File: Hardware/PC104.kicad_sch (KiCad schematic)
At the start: 13 parts, among them J2 ESQ-126-14-G-D, J3 ESQ-126-14-G-D

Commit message: STM32 RTC
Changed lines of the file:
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@@
 	)
 	(junction
-		(at 248.92 88.9)
+		(at 251.46 88.9)
 		(diameter 0)
 		(color 0 0 0 0)
@@
 	)
 	(junction
-		(at 207.01 160.02)
+		(at 251.46 96.52)
 		(diameter 0)
 		(color 0 0 0 0)
 	)
 	(junction
-		(at 125.73 83.82)
+		(at 207.01 160.02)
 		(diameter 0)
 		(color 0 0 0 0)
 	)
 	(junction
-		(at 248.92 81.28)
+		(at 125.73 83.82)
 		(diameter 0)
 		(color 0 0 0 0)
 	)
 	(junction
-		(at 248.92 96.52)
+		(at 251.46 81.28)
 		(diameter 0)
 		(color 0 0 0 0)
@@
 	(wire
 		(pts
-			(xy 248.92 81.28) (xy 260.35 81.28)
+			(xy 251.46 81.28) (xy 260.35 81.28)
 		)
 		(stroke
@@
 	(wire
 		(pts
-			(xy 246.38 96.52) (xy 248.92 96.52)
+			(xy 246.38 96.52) (xy 251.46 96.52)
 		)
 		(stroke
@@
 	(wire
 		(pts
-			(xy 246.38 81.28) (xy 248.92 81.28)
+			(xy 246.38 81.28) (xy 251.46 81.28)
 		)
 		(stroke
@@
 	(wire
 		(pts
-			(xy 248.92 96.52) (xy 260.35 96.52)
-		)
-		(stroke
-			(width 0)
-			(type default)
-		)
-	)
-	(wire
-		(pts
 			(xy 198.12 177.8) (xy 198.12 180.34)
 		)
@@
 	(wire
 		(pts
-			(xy 246.38 88.9) (xy 248.92 88.9)
+			(xy 246.38 88.9) (xy 251.46 88.9)
 		)
 		(stroke
@@
 	(wire
 		(pts
+			(xy 251.46 96.52) (xy 260.35 96.52)
+		)
+		(stroke
+			(width 0)
+			(type default)
+		)
+	)
+	(wire
+		(pts
 			(xy 288.29 88.9) (xy 288.29 96.52)
 		)
@@
 	(wire
 		(pts
-			(xy 248.92 88.9) (xy 260.35 88.9)
+			(xy 251.46 88.9) (xy 260.35 88.9)
 		)
 		(stroke
@@
 	(wire
 		(pts
-			(xy 240.03 116.84) (xy 240.03 123.19)
+			(xy 240.03 116.84) (xy 240.03 121.92)
 		)
 		(stroke
@@
 	(hierarchical_label "VBAT_MONITOR"
 		(shape input)
-		(at 240.03 123.19 180)
+		(at 240.03 121.92 180)
 		(effects
 			(font
@@
 	(symbol
 		(lib_id "power:PWR_FLAG")
-		(at 248.92 96.52 0)
+		(at 251.46 96.52 0)
 		(unit 1)
 		(exclude_from_sim no)
@@
 		(fields_autoplaced yes)
 		(property "Reference" "#FLG04"
-			(at 248.92 94.615 0)
+			(at 251.46 94.615 0)
 			(effects
 				(font
@@
 		)
 		(property "Value" "PWR_FLAG"
-			(at 248.92 91.44 0)
+			(at 251.46 91.44 0)
 			(effects
 				(font
@@
 		)
 		(property "Footprint" ""
-			(at 248.92 96.52 0)
+			(at 251.46 96.52 0)
 			(effects
 				(font
@@
 		)
 		(property "Datasheet" "~"
-			(at 248.92 96.52 0)
+			(at 251.46 96.52 0)
 			(effects
 				(font
@@
 		)
 		(property "Description" "Special symbol for telling ERC where power comes from"
-			(at 248.92 96.52 0)
+			(at 251.46 96.52 0)
 			(effects
 				(font
@@
 	(symbol
 		(lib_id "power:PWR_FLAG")
-		(at 248.92 81.28 0)
+		(at 251.46 81.28 0)
 		(unit 1)
 		(exclude_from_sim no)
@@
 		(fields_autoplaced yes)
 		(property "Reference" "#FLG02"
-			(at 248.92 79.375 0)
+			(at 251.46 79.375 0)
 			(effects
 				(font
@@
 		)
 		(property "Value" "PWR_FLAG"
-			(at 248.92 76.2 0)
+			(at 251.46 76.2 0)
 			(effects
 				(font
@@
 		)
 		(property "Footprint" ""
-			(at 248.92 81.28 0)
+			(at 251.46 81.28 0)
 			(effects
 				(font
@@
 		)
 		(property "Datasheet" "~"
-			(at 248.92 81.28 0)
+			(at 251.46 81.28 0)
 			(effects
 				(font
@@
 		)
 		(property "Description" "Special symbol for telling ERC where power comes from"
-			(at 248.92 81.28 0)
+			(at 251.46 81.28 0)
 			(effects
 				(font
@@
 	(symbol
 		(lib_id "power:PWR_FLAG")
-		(at 248.92 88.9 0)
+		(at 251.46 88.9 0)
 		(unit 1)
 		(exclude_from_sim no)
@@
 		(fields_autoplaced yes)
 		(property "Reference" "#FLG03"
-			(at 248.92 86.995 0)
+			(at 251.46 86.995 0)
 			(effects
 				(font
@@
 		)
 		(property "Value" "PWR_FLAG"
-			(at 248.92 83.82 0)
+			(at 251.46 83.82 0)
 			(effects
 				(font
@@
 		)
 		(property "Footprint" ""
-			(at 248.92 88.9 0)
+			(at 251.46 88.9 0)
 			(effects
 				(font
@@
 		)
 		(property "Datasheet" "~"
-			(at 248.92 88.9 0)
+			(at 251.46 88.9 0)
 			(effects
 				(font
@@
 		)
 		(property "Description" "Special symbol for telling ERC where power comes from"
-			(at 248.92 88.9 0)
+			(at 251.46 88.9 0)
 			(effects
 				(font

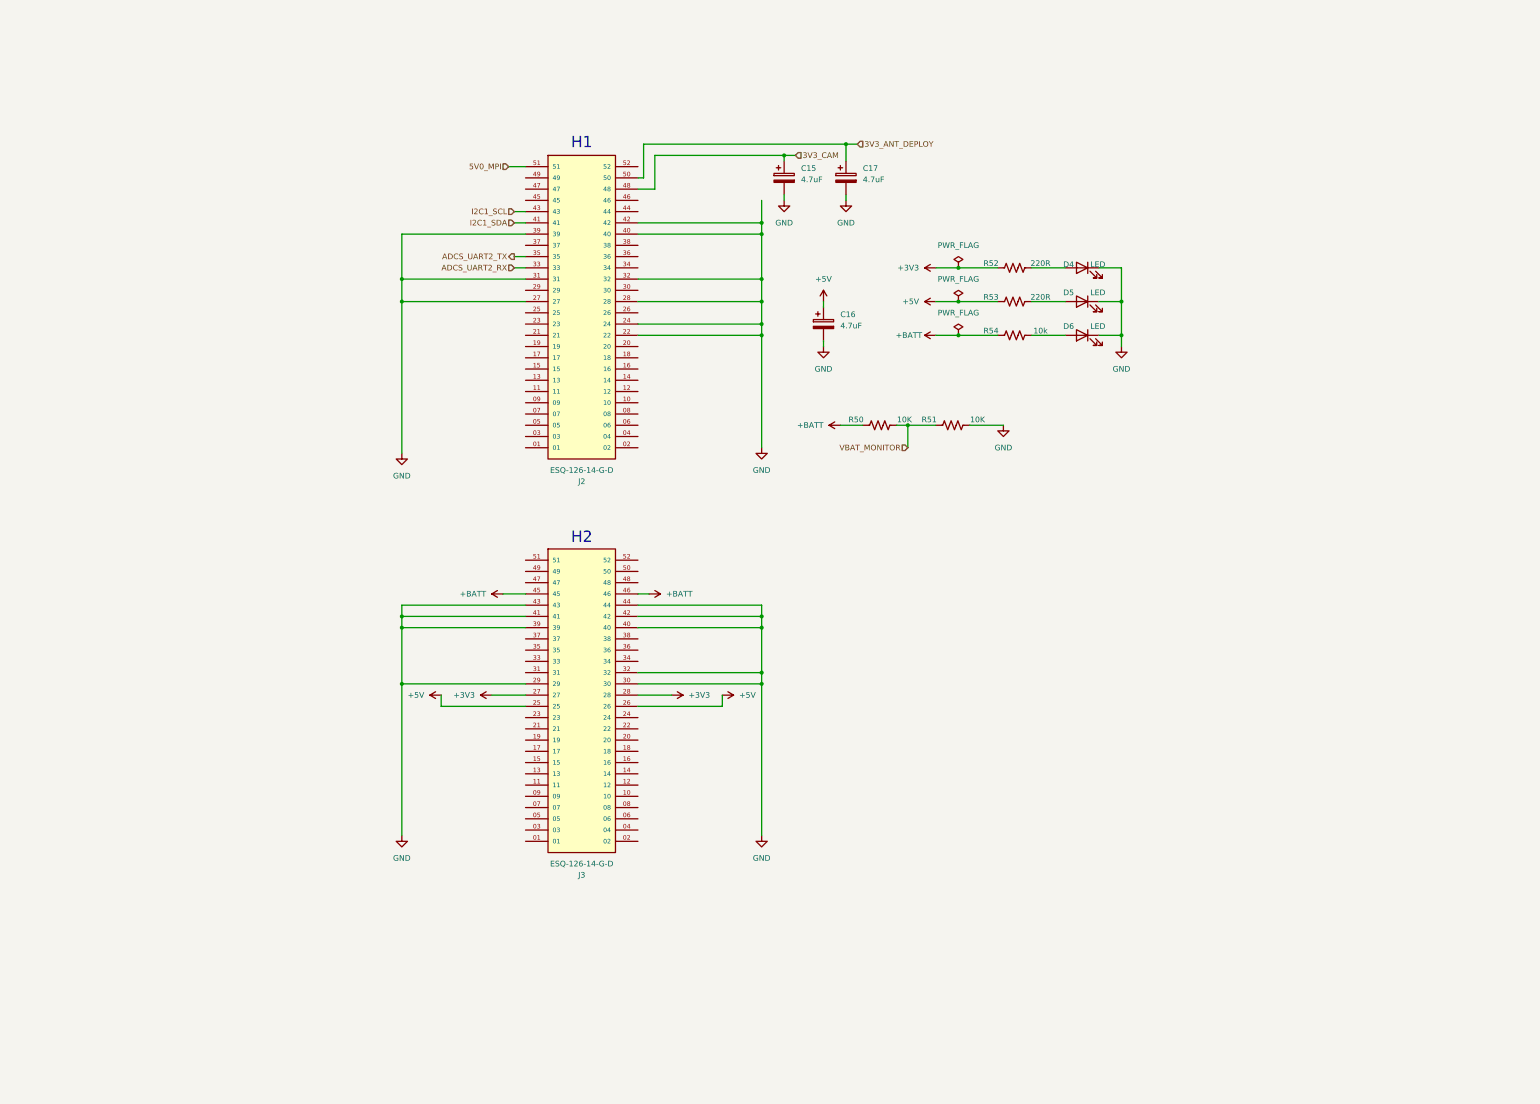
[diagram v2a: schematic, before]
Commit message: Begin with connectors
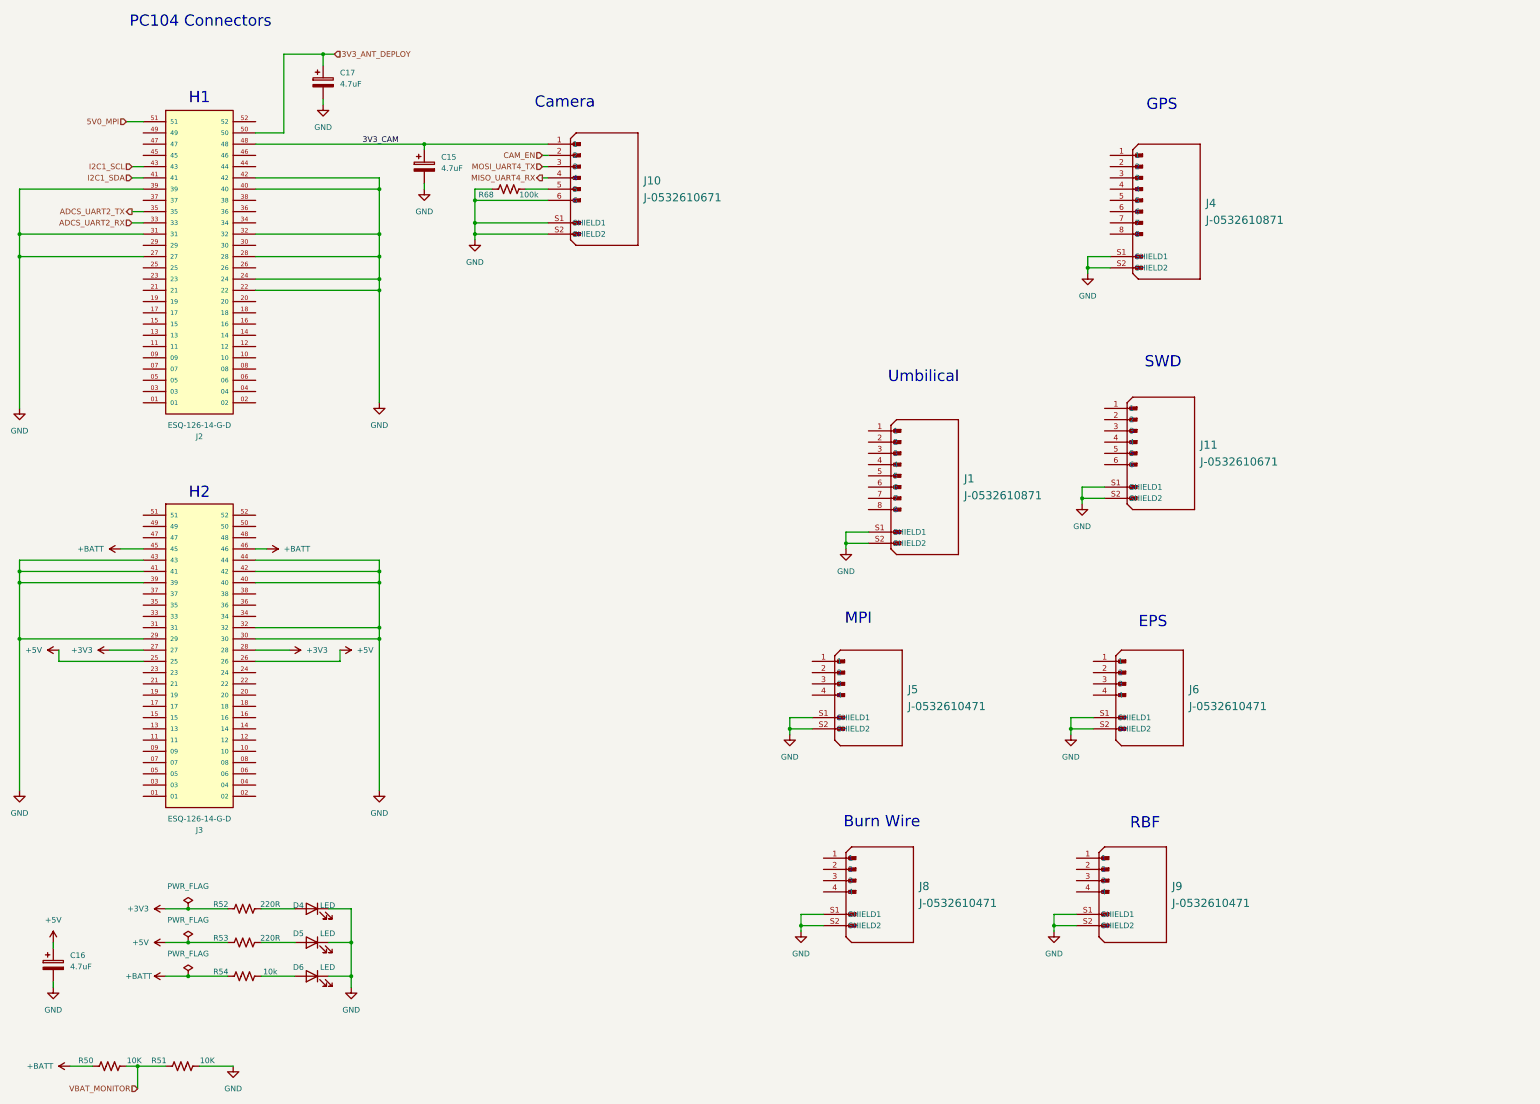
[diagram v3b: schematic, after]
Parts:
- added J1, J4: J-0532610871, J-532610871, symbol CTS-SAT-1 PCB:J-0532610871
- added J10, J11: J-0532610671, J-0532610671, symbol CTS-SAT-1 PCB:J-0532610671
- added J5, J6, J8, J9: J-0532610471, J-53261-0471, symbol CTS-SAT-1 PCB:J-0532610471
- added R68: 100k, symbol Device:R_US
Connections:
- net 3V3_CAM: now also J10.1
- net GND: now also J1.S1 (SHIELD1), J1.S2 (SHIELD2), J10.6, J10.S1 (SHIELD1), J10.S2 (SHIELD2), J11.S1 (SHIELD1), J11.S2 (SHIELD2), J4.S1 (SHIELD1), J4.S2 (SHIELD2), J5.S1 (SHIELD1), J5.S2 (SHIELD2), J6.S1 (SHIELD1), J6.S2 (SHIELD2), J8.S1 (SHIELD1), J8.S2 (SHIELD2), J9.S1 (SHIELD1), J9.S2 (SHIELD2), R68.1
- new net: J10.5, R68.2
- new net CAM_EN: J10.2
- new net MISO_UART4_RX: J10.4
- new net MOSI_UART4_TX: J10.3
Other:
- note added: "Burn Wire"
- note added: "Camera"
- note added: "EPS"
- note added: "GPS"
- note added: "MPI"
- note added: "PC104 Connectors"
- note added: "RBF"
- note added: "SWD"
- note added: "Umbilical"
- moved on the sheet: C15, C16, C17, D4, D5, D6, J2, J3, R50, R51, R52, R53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

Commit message: Begin importing to SAT-2 PCB
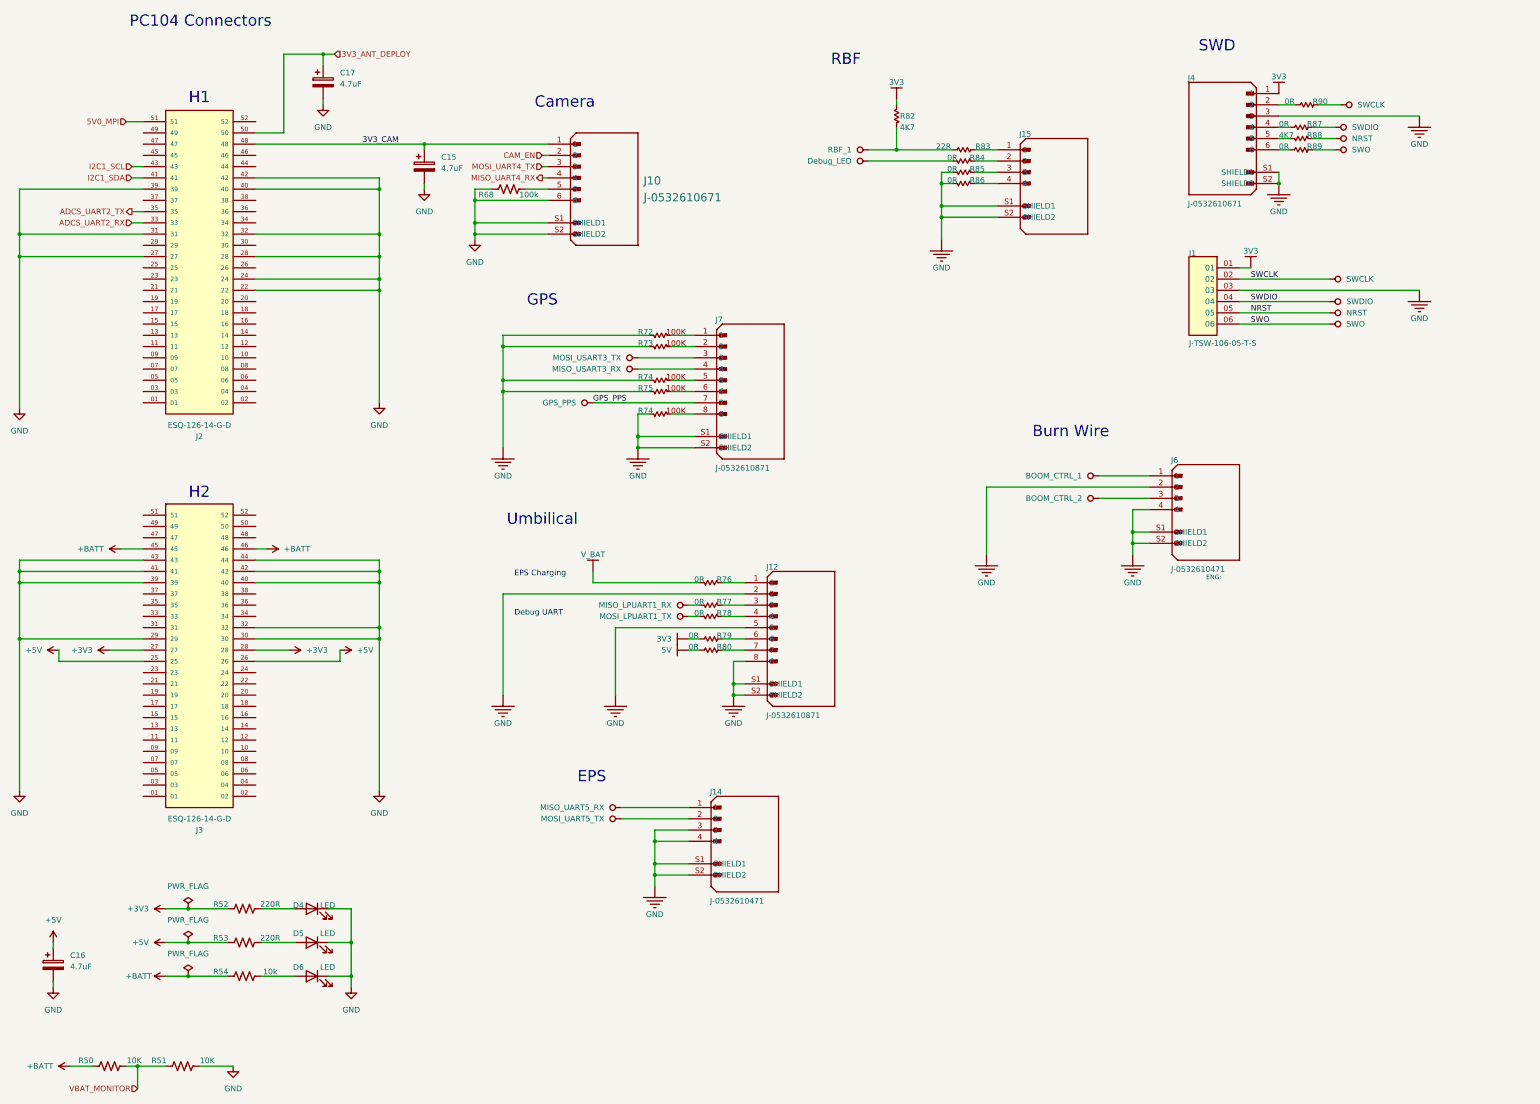
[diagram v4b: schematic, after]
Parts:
- removed J1, J4: J-0532610871, J-532610871, symbol CTS-SAT-1 PCB:J-0532610871
- removed J11: J-0532610671, J-0532610671, symbol CTS-SAT-1 PCB:J-0532610671
- removed J5, J6, J8, J9: J-0532610471, J-53261-0471, symbol CTS-SAT-1 PCB:J-0532610471
- added J1: J-TSW-106-05-T-S, J-TSW-106-05-T-S, symbol OBC Development Board:root_0_mirrored_J-TSW-106-05-T-S_OBC Development Board.Sc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
- added J12, J7: J-0532610871, J-532610871, symbol OBC Development Board:root_0_J-0532610871_OBC Development Board.SchLib
- added J14, J15, J6: J-0532610471, J-53261-0471, symbol OBC Development Board:root_0_J-0532610471_OBC Development Board.SchLib
- added J4: J-0532610671, J-0532610671, symbol OBC Development Board:root_0_mirrored_J-0532610671_OBC Development Board.SchLib
- added R72, R73, R74 (x2), R75: 100K, 0603, symbol OBC Development Board:root_0_RT-100K0-F-1/16W-0603_OBC Development Board.SchLib
- added R76, R77, R78, R84, R85, R86: 0R, 0603, symbol OBC Development Board:root_0_RT-0R00-F-1/10W-0603_OBC Development Board.SchLib
- added R79, R80, R87, R89, R90: 0R, 0603, symbol OBC Development Board:root_0_mirrored_RT-0R00-F-1/10W-0603_OBC Development Boar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
- added R82: 4K7, 0603, symbol OBC Development Board:root_1_RT-4K7-F-1/16W-0603_OBC Development Board.SchLib
- added R83: 22R, 0603, symbol OBC Development Board:root_2_mirrored_RT-22R0-F-1/16W-0603_OBC Development Boar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
- added R88: 4K7, 0603, symbol OBC Development Board:root_2_RT-4K7-F-1/16W-0603_OBC Development Board.SchLib
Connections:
- net GND: now also J1.03, J12.2, J12.5, J12.8, J12.S1 (SHIELD1), J12.S2 (SHIELD2), J14.3, J14.4, J14.S1 (SHIELD1), J14.S2 (SHIELD2), J15.S1 (SHIELD1), J15.S2 (SHIELD2), J4.3, J4.S1 (SHIELD1), J4.S2 (SHIELD2), J6.2, J6.4, J6.S1 (SHIELD1), J6.S2 (SHIELD2), J7.S1 (SHIELD1), J7.S2 (SHIELD2), R72.1, R73.1, R74.1, R74.1, R75.1, R85.1, R86.1
- new net: J15.3, R85.2
- new net: J15.2, R84.2
- new net: J4.6, R89.2
- new net: J4.2, R90.2
- new net: J4.4, R87.2
- new net: J4.5, R88.2
- new net: J15.1, R83.2
- new net: J15.4, R86.2
- new net: J12.3, R77.2
- new net: J7.6, R75.2
- new net: J7.5, R74.2
- new net: J12.7, R80.1
- new net: J12.4, R78.2
- new net: J7.1, R72.2
- new net: J7.8, R74.2
- new net: J12.6, R79.1
- new net: J7.2, R73.2
- new net: J12.1, R76.2
- new net 3V3: J1.01, J4.1, R79.2, R82.2
- new net 5V: R80.2
- new net BOOM_CTRL_1: J6.1
- new net BOOM_CTRL_2: J6.3
- new net Debug_LED: R84.1
- new net GPS_PPS: J7.7
- new net MISO_LPUART1_RX: R77.1
- new net MISO_UART5_RX: J14.1
- new net MISO_USART3_RX: J7.4
- new net MOSI_LPUART1_TX: R78.1
- new net MOSI_UART5_TX: J14.2
- new net MOSI_USART3_TX: J7.3
- new net NRST: J1.05, R88.1
- new net RBF_1: R82.1, R83.1
- new net SWCLK: J1.02, R90.1
- new net SWDIO: J1.04, R87.1
- new net SWO: J1.06, R89.1
- new net V_BAT: R76.1
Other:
- note added: "Debug UART"
- note added: "ENG:"
- note added: "EPS Charging"
- note removed: "MPI"

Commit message: Connect connectors
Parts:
- removed R68: 100k, symbol Device:R_US
- removed R72, R73, R74 (x2), R75: 100K, 0603, symbol OBC Development Board:root_0_RT-100K0-F-1/16W-0603_OBC Development Board.SchLib
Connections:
- net 5V is gone; now on net +5V: R80.2
- net Debug_LED renamed DEBUG_LED

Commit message: Add STM32 Reset Switch & RP2040 I2C pins
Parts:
- renumbered C16 to C36, C17 to C37, C15 to C38, J2 to J1, J4 to J10, J3 to J2, J10 to J3, J14 to J4, J7 to J5, J12 to J6, J15 to J7, J1 to J8, J6 to J9, R50 to R53, R51 to R54, R52 to R55, R53 to R56, R54 to R57, R76 to R58, R77 to R59, R78 to R60, R79 to R61, R80 to R62, R82 to R63, R83 to R64, R84 to R65, R85 to R66, R86 to R67, R87 to R68, R88 to R69, R89 to R70, R90 to R71

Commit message: Add RP2040 SWD
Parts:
- added J12: J-TSW-106-05-T-S, J-TSW-106-05-T-S, symbol OBC Development Board:root_0_mirrored_J-TSW-106-05-T-S_OBC Development Board.Sc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
- added J13: J-0532610671, J-0532610671, symbol OBC Development Board:root_0_mirrored_J-0532610671_OBC Development Board.SchLib
- added R69, R70: 0R, 0603, symbol OBC Development Board:root_0_mirrored_RT-0R00-F-1/10W-0603_OBC Development Boar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
- added R71: 4K7, 0603, symbol OBC Development Board:root_2_RT-4K7-F-1/16W-0603_OBC Development Board.SchLib
- renumbered J9 to J10, J7 to J11, J1 to J2, J2 to J3, J3 to J4, J4 to J5, J5 to J6, J6 to J7, J10 to J9, R53 to R50, R54 to R51, R55 to R52, R56 to R53, R57 to R54, R58 to R55, R59 to R56, R60 to R57, R61 to R58, R62 to R59, R63 to R60, R64 to R61, R65 to R62, R66 to R63, R67 to R64, R71 to R65, R68 to R66, R69 to R67, R70 to R68
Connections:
- net 3V3: now also J12.01, J13.1
- net GND: now also J12.03, J13.3, J13.S1 (SHIELD1), J13.S2 (SHIELD2)
- net NRST renamed RP2040_NRST
- net RP2040_NRST: now also J12.05, R71.1
- net SWCLK renamed RP2040_SWCLK
- net RP2040_SWCLK: now also J12.02, R69.1
- net SWDIO renamed RP2040_SWDIO
- net RP2040_SWDIO: now also J12.04, R70.1
- net SWO renamed RP2040_~{BOOTSEL}
- net RP2040_~{BOOTSEL}: now also J12.06, J13.6
- new net: J13.5, R71.2
- new net: J13.4, R70.2
- new net: J13.2, R69.2
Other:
- note added: "RP2040 SWD"
- note added: "STM32 SWD"
- note removed: "SWD"
- moved on the sheet: J10, J11, J8, J9, R60, R61, R62, R63, R64, R65, R66, R67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

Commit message: Finish schematic v1
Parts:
- added J17: J-0532610471, J-53261-0471, symbol OBC Development Board:root_0_J-0532610471_OBC Development Board.SchLib
- added J2, J5, J6: 2-Pin Header, symbol Connector_Generic:Conn_02x01
- renumbered J7 to J10, J8 to J11, J9 to J12, J10 to J13, J11 to J14, J12 to J15, J13 to J16, J2 to J3, J3 to J4, J4 to J7, J5 to J8, J6 to J9
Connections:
- net +3V3: now also J2.1 (Pin_1); no longer J4.27
- net +5V: now also J6.2 (Pin_2); no longer J4.26
- net +BATT: now also J5.2 (Pin_2); no longer J4.46
- net GND: now also J17.3, J17.4, J17.S1 (SHIELD1), J17.S2 (SHIELD2)
- net ADCS_UART2_RX renamed ADCS_UART_RX
- net ADCS_UART2_TX renamed ADCS_UART_TX
- new net: J4.26, J6.1 (Pin_1)
- new net: J2.2 (Pin_2), J4.27
- new net: J4.46, J5.1 (Pin_1)
- new net MISO_USART2_RX: J17.2
- new net MOSI_USART2_TX: J17.1
- no-connect marks 0 -> 2
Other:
- note added: "Optical Downlink"
- note removed: "ENG:"
